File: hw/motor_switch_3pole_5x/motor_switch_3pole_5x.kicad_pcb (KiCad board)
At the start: 2 copper layers, 93 x 89.6 mm, 116 parts, among them J1 CONN_2X1, J10 WAGO 233-504, J11 WAGO 233-504, J12 CONN-ISP-6, J13 WAGO 243-723, J14 WAGO 243-724, J15 WAGO 243-721, J16 WAGO 243-722, J17 CONN_1, J18 CONN_1, J2 WAGO 2081-1122, J3 WAGO 2081-1122, J4 WAGO 2081-1122, J5 WAGO 2081-1122, J6 WAGO 2081-1122, J7 WAGO 233-504, J8 WAGO 233-504, J9 WAGO 233-504, Q1 BSS138, Q10 BSS138, Q2 BSS138, Q3 BSS138, Q4 BSS138, Q5 BSS138, Q6 BSS138, Q7 BSS138, Q8 BSS138, Q9 BSS138, U1 74HC595, U2 74HC595, U3 25LC256, U4 ATMEGA328-TQFP32, U5 7,3728MHz, U6 MAX487ECSA, U7 AM1S-2405

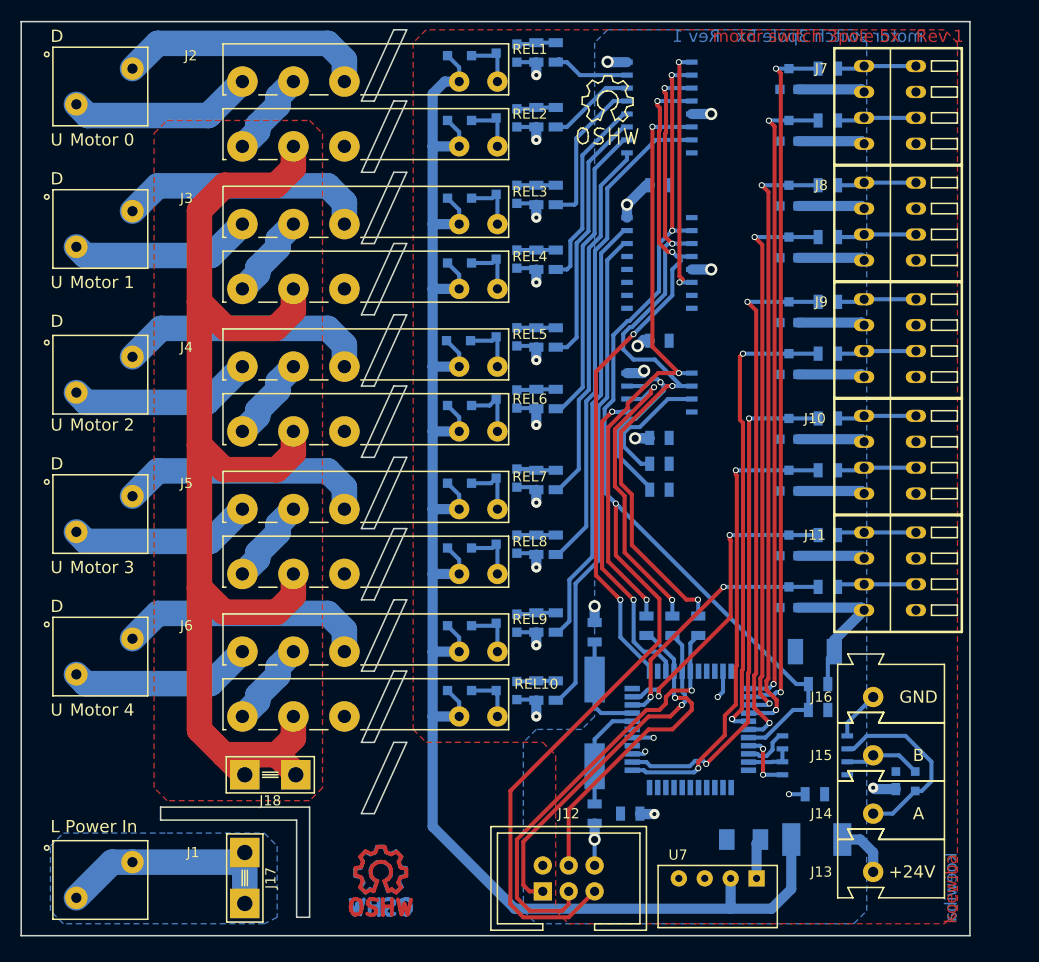
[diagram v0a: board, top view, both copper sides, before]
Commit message: Fix: Size of vias and DRC issues
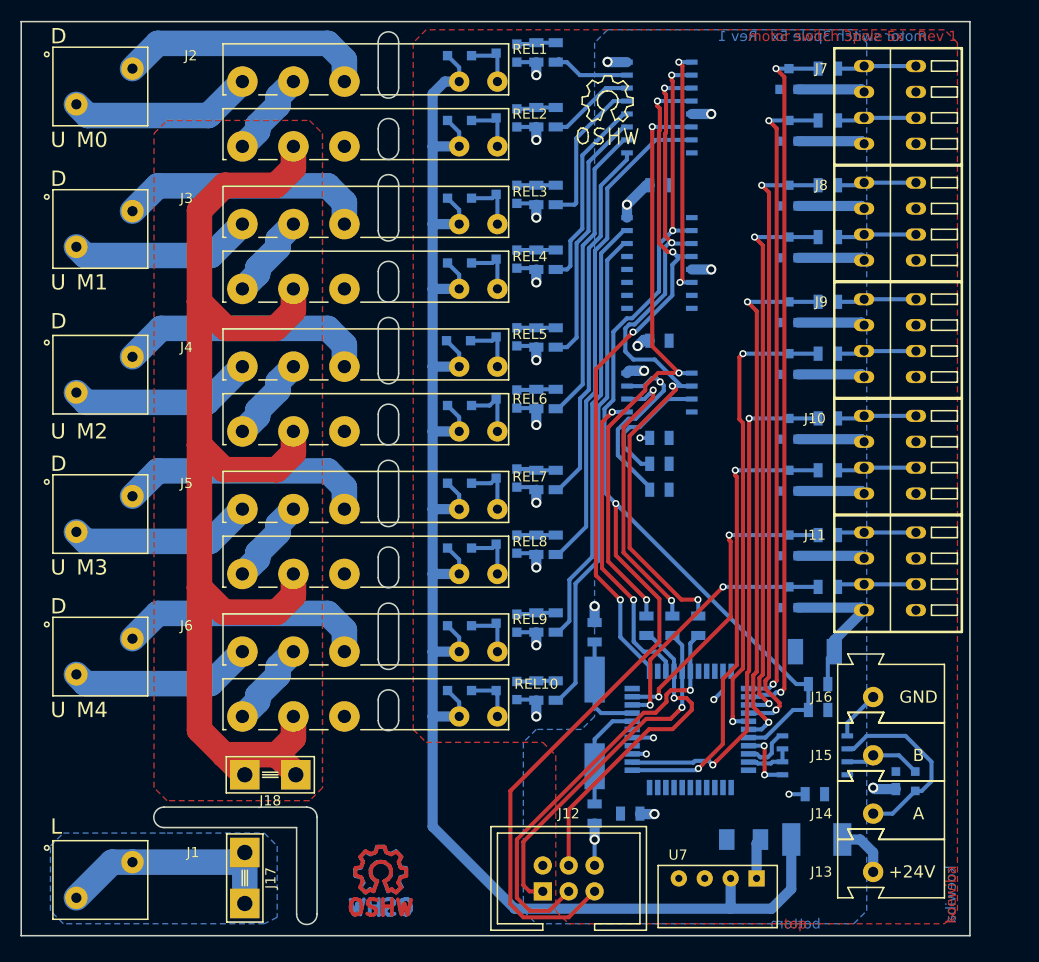
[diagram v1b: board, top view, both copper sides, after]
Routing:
- net /bus_atmega328_basic/MISO: track 29.5 -> 28.3 mm
- net /bus_atmega328_basic/PB5_SCK: track 42.2 -> 41.3 mm
- net //button_4_up: track 30.8 -> 30.2 mm
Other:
- outline, holes or cut-outs redrawn
- net class Default: via_dia 0.6 -> 0.7
- net class Power: clearance 0.3 -> 0.2; via_drill 0.4 -> 0.6
- rule via_min_size: 0.4 -> 0.7
- board text added: "L"
- board text added: "M0"
- board text added: "M1"
- board text added: "M2"
- board text added: "M3"
- board text added: "M4"
- board text added: "bottom"
- board text added: "top"
- board text removed: "L Power In"
- board text removed: "Motor 0"
- board text removed: "Motor 1"
- board text removed: "Motor 2"
- board text removed: "Motor 3"
- board text removed: "Motor 4"

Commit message: Moved motor connectors to avoid THT pad touching the housing
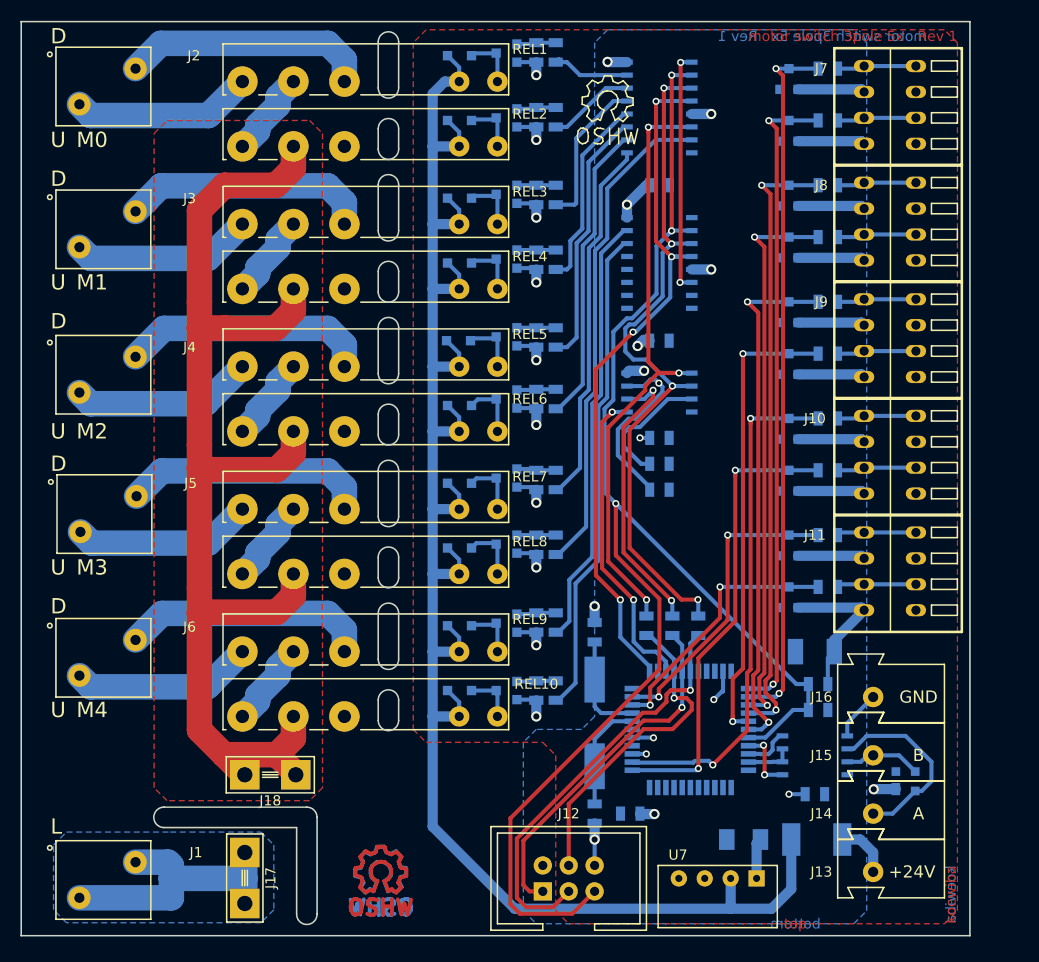
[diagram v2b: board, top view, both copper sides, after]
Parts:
- moved J5 0.40 mm to (111.3, 96.5)
- moved J6 0.32 mm to (111.2, 110.6)
- moved J3 0.30 mm to (111.2, 68.6)
- moved J1 0.30 mm to (111.2, 132.4)
- moved J2 0.30 mm to (111.2, 54.6)
- moved J4 0.30 mm to (111.2, 82.9)
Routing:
- net Net-(J1-Pad1): track 23.3 -> 28.0 mm
- net /Motor Relays/230V: track 121.7 -> 118.8 mm
- net /output_data: track 59.8 -> 61.4 mm
- net /output_latch: track 67.6 -> 68.3 mm

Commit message: added LEDs and testpoints to PCB
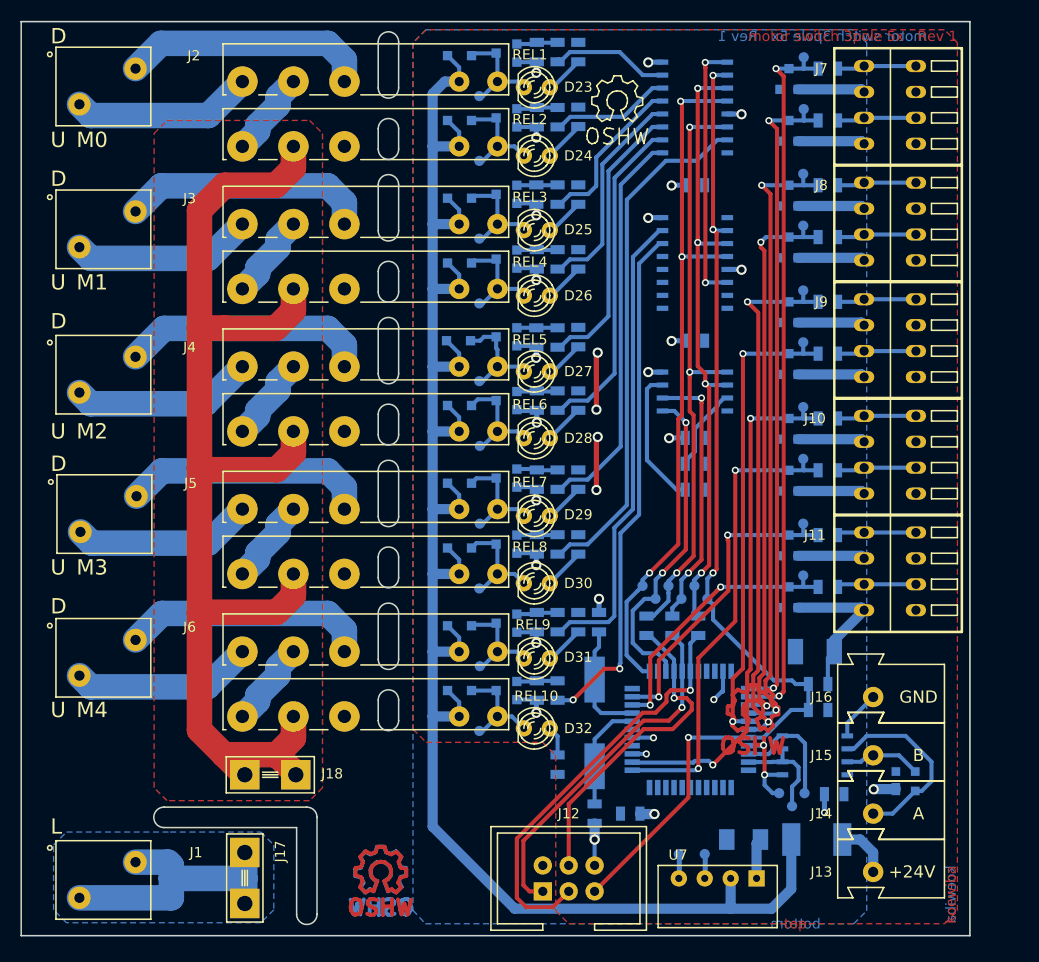
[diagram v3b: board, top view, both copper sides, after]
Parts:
- added D23: yellow, 2,1V/2mA, LED:LED_RM2.54mm_D3mm, F.Cu at (150.5, 56.4)
- added D24: green, 2,2V/2mA, LED:LED_RM2.54mm_D3mm, F.Cu at (150.5, 63.1)
- added D25: yellow, 2,1V/2mA, LED:LED_RM2.54mm_D3mm, F.Cu at (150.5, 70.4)
- added D26: green, 2,2V/2mA, LED:LED_RM2.54mm_D3mm, F.Cu at (150.5, 76.9)
- added D27: yellow, 2,1V/2mA, LED:LED_RM2.54mm_D3mm, F.Cu at (150.5, 84.3)
- added D28: green, 2,2V/2mA, LED:LED_RM2.54mm_D3mm, F.Cu at (150.5, 90.8)
- added D29: yellow, 2,1V/2mA, LED:LED_RM2.54mm_D3mm, F.Cu at (150.5, 98.5)
- added D30: green, 2,2V/2mA, LED:LED_RM2.54mm_D3mm, F.Cu at (150.5, 105.1)
- added D31: yellow, 2,1V/2mA, LED:LED_RM2.54mm_D3mm, F.Cu at (150.5, 112.4)
- added D32: green, 2,2V/2mA, LED:LED_RM2.54mm_D3mm, F.Cu at (150.5, 119.3)
- added J19: tp_output_motor_0_up, Connector_Miscelleaneus:Testpoint_1mm, B.Cu at (145.0, 57.3)
- added J20: tp_output_motor_on, Connector_Miscelleaneus:Testpoint_1mm, B.Cu at (145.0, 63.7)
- added J21: tp_output_motor_1_up, Connector_Miscelleaneus:Testpoint_1mm, B.Cu at (145.0, 71.3)
- added J22: tp_output_motor_1_on, Connector_Miscelleaneus:Testpoint_1mm, B.Cu at (145.0, 77.6)
- added J23: tp_output_motor_2_up, Connector_Miscelleaneus:Testpoint_1mm, B.Cu at (145.0, 85.2)
- added J24: tp_output_motor_2_on, Connector_Miscelleaneus:Testpoint_1mm, B.Cu at (145.0, 91.6)
- added J25: tp_output_motor_3_up, Connector_Miscelleaneus:Testpoint_1mm, B.Cu at (145.0, 99.2)
- added J26: tp_output_motor_3_on, Connector_Miscelleaneus:Testpoint_1mm, B.Cu at (145.0, 105.6)
- added J27: tp_output_motor_4_up, Connector_Miscelleaneus:Testpoint_1mm, B.Cu at (145.0, 113.2)
- added J28: tp_output_motor_4_on, Connector_Miscelleaneus:Testpoint_1mm, B.Cu at (145.0, 119.5)
- added J29: tp_cseep, Connector_Miscelleaneus:Testpoint_1mm, B.Cu at (162.2, 106.6)
- added J30: tp_vcc, Connector_Miscelleaneus:Testpoint_1mm, B.Cu at (164.5, 131.6)
- added J31: tp_gnd, Connector_Miscelleaneus:Testpoint_1mm, B.Cu at (167.1, 131.6)
- added J32: tp_output_button_0_up, Connector_Miscelleaneus:Testpoint_1mm, B.Cu at (176.8, 53.5)
- added J33: tp_output_button_0_down, Connector_Miscelleaneus:Testpoint_1mm, B.Cu at (176.8, 58.6)
- added J34: tp_output_button_1_up, Connector_Miscelleaneus:Testpoint_1mm, B.Cu at (176.7, 64.9)
- added J35: tp_output_button_1_down, Connector_Miscelleaneus:Testpoint_1mm, B.Cu at (176.7, 70.0)
- added J36: tp_output_button_2_up, Connector_Miscelleaneus:Testpoint_1mm, B.Cu at (176.7, 76.4)
- added J37: tp_output_button_2_down, Connector_Miscelleaneus:Testpoint_1mm, B.Cu at (176.7, 81.4)
- added J38: tp_output_button_3_up, Connector_Miscelleaneus:Testpoint_1mm, B.Cu at (176.7, 87.8)
- added J39: tp_output_button_3_down, Connector_Miscelleaneus:Testpoint_1mm, B.Cu at (176.7, 92.9)
- added J40: tp_output_button_4_up, Connector_Miscelleaneus:Testpoint_1mm, B.Cu at (176.7, 99.2)
- added J41: tp_output_button_4_down, Connector_Miscelleaneus:Testpoint_1mm, B.Cu at (176.7, 104.3)
- added J42: tp_output_latch, Connector_Miscelleaneus:Testpoint_1mm, B.Cu at (161.0, 105.3)
- added J43: tp_output_data, Connector_Miscelleaneus:Testpoint_1mm, B.Cu at (163.5, 105.3)
- added J44: tp_output_clock, Connector_Miscelleaneus:Testpoint_1mm, B.Cu at (166.0, 105.3)
- added J45: tp_output_reset, Connector_Miscelleaneus:Testpoint_1mm, B.Cu at (167.3, 106.6)
- added J46: tp_miso, Connector_Miscelleaneus:Testpoint_1mm, B.Cu at (164.8, 106.6)
- added J47: tp_txden, Connector_Miscelleaneus:Testpoint_1mm, B.Cu at (175.6, 126.9)
- added J48: tp_txd, Connector_Miscelleaneus:Testpoint_1mm, B.Cu at (176.8, 125.6)
- added J49: tp_rxd, Connector_Miscelleaneus:Testpoint_1mm, B.Cu at (174.3, 125.6)
- added LOGO3: OPEN_HARDWARE_1, Symbol:Symbol_OSHW-Logo_Copper, F.Cu at (171.7, 117.5)
- added R37: 1k5, Resistor:R_0805, B.Cu at (154.6, 53.0)
- added R38: 1k5, Resistor:R_0805, B.Cu at (154.6, 59.3)
- added R39: 1k5, Resistor:R_0805, B.Cu at (154.6, 67.0)
- added R40: 1k5, Resistor:R_0805, B.Cu at (154.6, 73.3)
- added R41: 1k5, Resistor:R_0805, B.Cu at (154.6, 80.9)
- added R42: 1k5, Resistor:R_0805, B.Cu at (154.6, 87.1)
- added R43: 1k5, Resistor:R_0805, B.Cu at (154.6, 94.9)
- added R44: 1k5, Resistor:R_0805, B.Cu at (154.6, 101.2)
- added R45: 1k5, Resistor:R_0805, B.Cu at (154.6, 108.9)
- added R46: 1k5, Resistor:R_0805, B.Cu at (152.6, 122.8)
- moved U3 3.48 mm to (166.0, 86.3)
- moved C1 3.48 mm to (166.0, 66.0)
- moved C2 3.48 mm to (166.0, 81.3)
- moved C4 3.48 mm to (166.0, 90.8)
- moved R31 3.48 mm to (166.0, 95.9)
- moved R35 3.48 mm to (166.0, 93.3)
- moved U1 3.48 mm to (166.0, 58.4)
- moved U2 3.48 mm to (166.0, 73.7)
- moved C9 1.89 mm to (179.7, 125.7)
- moved C6 1.08 mm to (156.6, 108.9)
- moved LOGO4 0.94 mm to (158.4, 57.8)
- moved R12 0.24 mm to (152.6, 87.1)
- moved R10 0.18 mm to (152.6, 73.3)
- moved R17 0.18 mm to (152.6, 94.9)
- moved R18 0.18 mm to (152.6, 101.2)
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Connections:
- D22 pad 2: (no net) -> Net-(D22-Pad2)
- U2 pad 1: (no net) -> Net-(U2-Pad1)
- U2 pad 15: (no net) -> Net-(U2-Pad15)
- U2 pad 2: (no net) -> Net-(U2-Pad2)
- U2 pad 3: (no net) -> Net-(U2-Pad3)
- U2 pad 4: (no net) -> Net-(U2-Pad4)
- U2 pad 5: (no net) -> Net-(U2-Pad5)
- U2 pad 9: (no net) -> Net-(U2-Pad9)
- U4 pad 11: (no net) -> /bus_atmega328_basic/PD7
- U4 pad 13: (no net) -> /bus_atmega328_basic/PB1
- U4 pad 19: (no net) -> /bus_atmega328_basic/ADC6
- U4 pad 20: (no net) -> /bus_atmega328_basic/AREF
- U4 pad 22: (no net) -> /bus_atmega328_basic/ADC7
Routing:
- net /output_reset: track 141.8 -> 103.2 mm, vias 3 -> 4
- net +5V: track 0.00 -> 15.9 mm, vias 0 -> 4
- net /output_clock: track 70.2 -> 61.3 mm
- net /bus_atmega328_basic/TXD0: track 4.52 -> 11.9 mm
- net /bus_atmega328_basic/TXD0EN: track 4.61 -> 10.5 mm
- net Net-(D27-Pad2): track 5.64 -> 11.1 mm
- net Net-(D10-Pad1): track 5.19 -> 10.6 mm
- net Net-(D2-Pad1): track 5.36 -> 10.7 mm
- net Net-(D30-Pad2): track 5.63 -> 10.9 mm
- net Net-(D26-Pad2): track 5.54 -> 10.7 mm
- net Net-(D31-Pad2): track 5.36 -> 10.5 mm
- net Net-(D29-Pad2): track 5.72 -> 10.9 mm
- net Net-(D28-Pad2): track 5.90 -> 11.1 mm
- net Net-(D25-Pad2): track 5.54 -> 10.7 mm
- net Net-(D1-Pad1): track 5.36 -> 10.5 mm
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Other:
- net class Power: trace_width 1 -> 0.5
